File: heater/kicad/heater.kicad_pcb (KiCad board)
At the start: 2 copper layers, 90 x 88.4 mm, 82 parts, among them J1 Conn_01x02_Pin, J2 Conn_01x02_Pin, J3 pcie_98, U1 OPA863SIDBVR, U10 B0509XT-1WR3, U11 ESD5344D-TP, U12 ESD5344D-TP, U13 XC6206P332MR, U2 OPA863SIDBVR, U3 LTC1968, U4 LTC1968, U5 OPA863SIDBVR, U6 OPA863SIDBVR, U7 LP2985-5.0, U8 ADS1115IDGS, U9 ISO1541

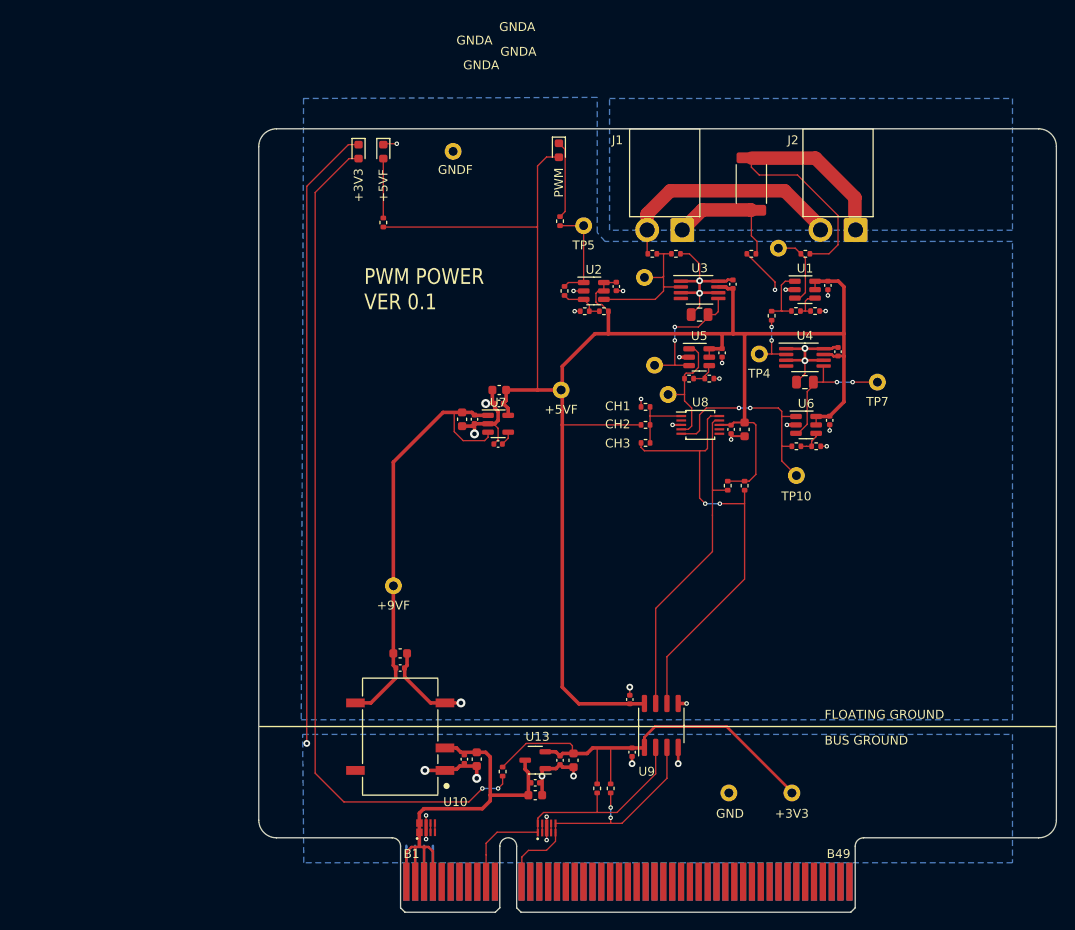
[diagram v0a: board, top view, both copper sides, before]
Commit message: Updated heater layout. Silk screeen labels are done.
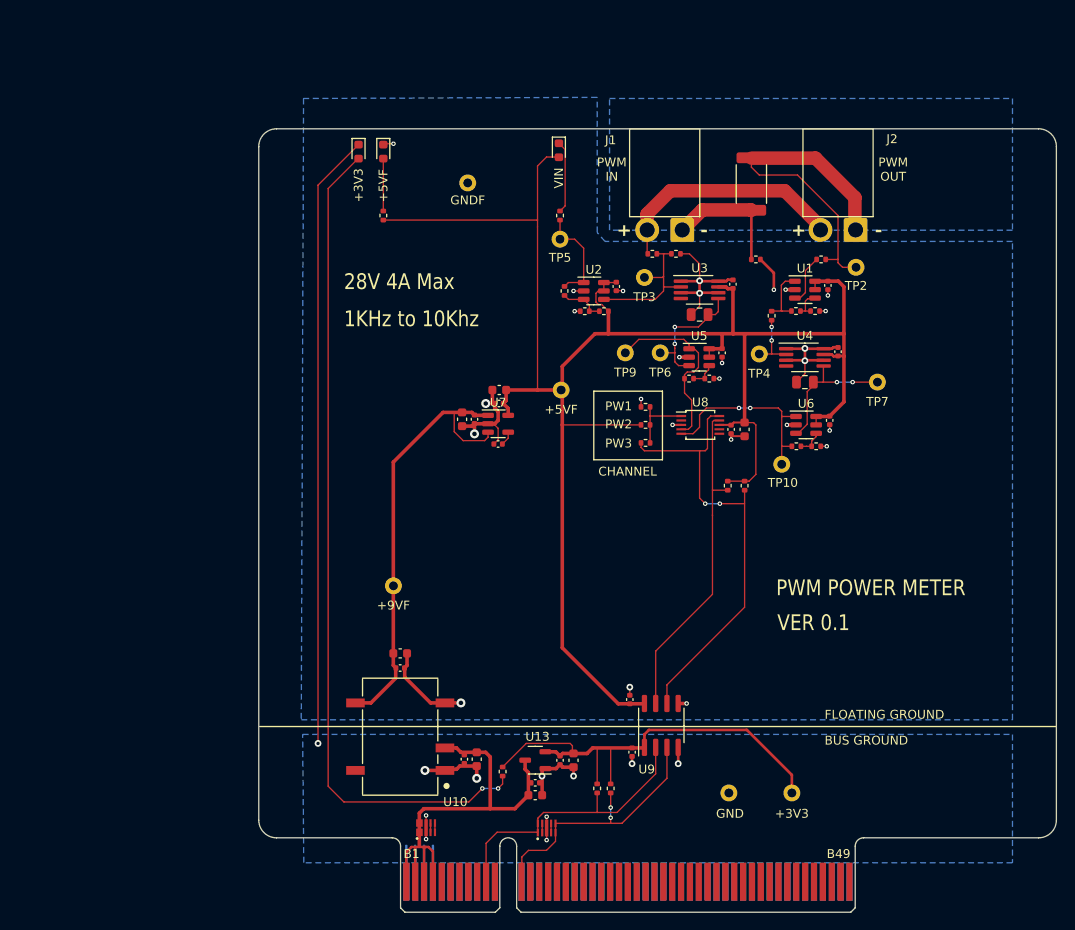
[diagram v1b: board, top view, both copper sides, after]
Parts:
- moved TP2 9.03 mm to (39.2, -72.8)
- moved TP9 6.74 mm to (13.2, -63.1)
- moved TP1 3.92 mm to (-4.57, -82.3)
- moved TP5 3.07 mm to (5.84, -75.9)
- moved TP10 2.08 mm to (30.9, -50.5)
- moved R6 1.89 mm to (35.3, -73.7)
- moved TP6 1.53 mm to (17.1, -63.1)
- moved R1 0.81 mm to (27.9, -73.7), turned to 0 degrees
- moved R5 0.79 mm to (-14.1, -78.6)
- moved R13 0.63 mm to (5.84, -78.6)
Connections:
- TP2 pad 1: Net-(U1-+) -> Net-(J2-Pin_1)
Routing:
- net Net-(U8-AIN0): track 14.1 -> 20.8 mm
- net Net-(U1-+): track 8.83 -> 5.71 mm
- net +5VF: track 211.4 -> 208.8 mm
- net Net-(U8-AIN1): track 24.4 -> 22.2 mm
- net Net-(J2-Pin_1): track 37.2 -> 39.2 mm
- net Net-(D3-A): track 96.2 -> 94.4 mm
- net GNDF: track 79.7 -> 78.0 mm
- net GND: track 109.8 -> 108.6 mm
- net +5V: track 49.6 -> 50.7 mm
- net +3V3: track 51.0 -> 52.0 mm
- net Net-(U3-OUT): track 15.1 -> 14.3 mm
- net Net-(D1-A): track 6.70 -> 5.92 mm
- net Net-(D2-K): track 8.81 -> 8.17 mm
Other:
- board text added: "+"
- board text added: "-"
- board text added: "1KHz to 10Khz"
- board text added: "28V 4A Max"
- board text added: "CHANNEL"
- board text added: "PW1"
- board text added: "PW2"
- board text added: "PW3"
- board text added: "PWM IN"
- board text added: "PWM OUT"
- board text added: "PWM POWER METER"
- board text added: "TO9"
- board text added: "TP2"
- board text added: "TP3"
- board text added: "TP6"
- board text added: "TP9"
- board text added: "VER 0.1"
- board text added: "VIN"
- board text removed: "CH1"
- board text removed: "CH2"
- board text removed: "CH3"
- board text removed: "GNDA"
- board text removed: "PWM"
- board text removed: "PWM POWER VER 0.1"

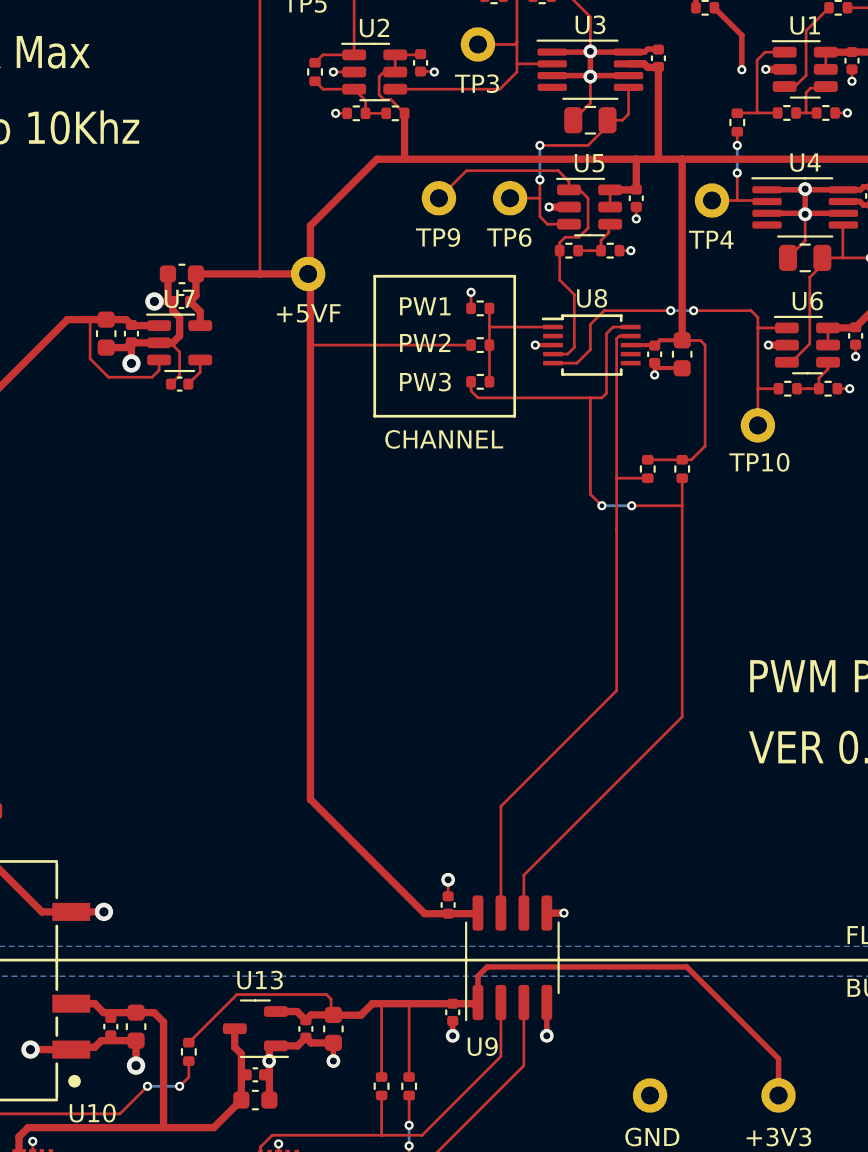
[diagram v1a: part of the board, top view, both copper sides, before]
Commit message: Adjusted for JLCPCB upload.
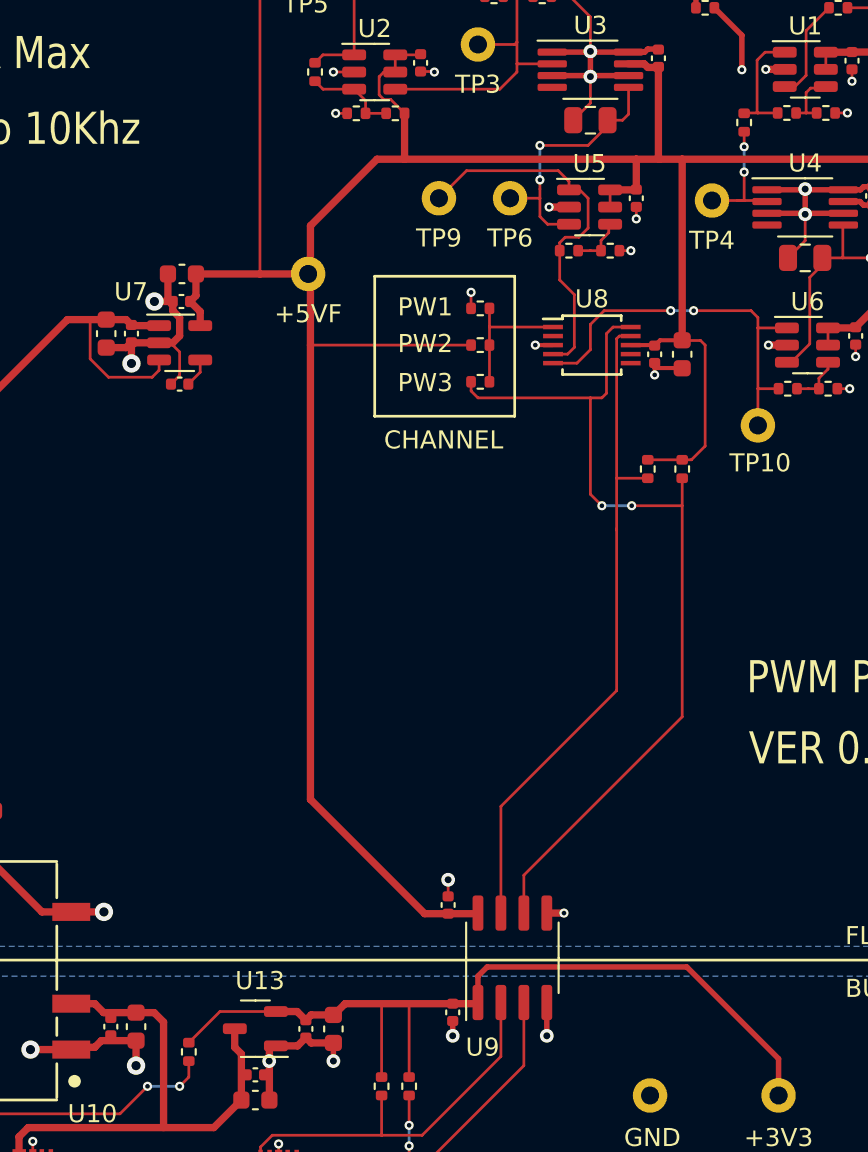
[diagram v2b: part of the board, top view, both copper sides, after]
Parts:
- moved R12 0.38 mm to (30.1, -67.3)
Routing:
- net +3V3: track 52.0 -> 47.7 mm
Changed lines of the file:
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@@
   )
   (footprint "Resistor_SMD:R_0402_1005Metric" (layer "F.Cu")
-    (at 29.718 -67.31 90)
+    (at 30.099 -67.31 90)
     (descr "Resistor SMD 0402 (1005 Metric), square (rectangular) end terminal, IPC_7351 nominal, (Body size source: IPC-SM-782 page 72, https://www.pcb-3d.com/wordpress/wp-content/uploads/ipc-sm-782a_amendment_1_and_2.pdf), generated with kicad-footprint-generator")
     (tags "resistor")
@@
     (descr "Isolated 1W or 2W Single Output SM DC/DC Converters https://www.murata.com/products/productdata/8807031865374/kdc-nxe1.pdf#page=8 https://www.murata.com/products/productdata/8807031898142/kdc-nxe2.pdf#page=9")
     (tags "Isolated 1W or 2W Single Output SM DC/DC Converters")
+    (property "JLCRotOffset" "270")
+    (property "LCSC" "C976389")
     (property "Sheetfile" "heater.kicad_sch")
     (property "Sheetname" "")
@@
     (descr "SOT, 5 Pin (https://www.jedec.org/sites/default/files/docs/Mo-178c.PDF variant AA), generated with kicad-footprint-generator ipc_gullwing_generator.py")
     (tags "SOT TO_SOT_SMD")
+    (property "JLCRotOffset" "180")
     (property "LCSC" "C130188")
     (property "Sheetfile" "heater.kicad_sch")
@@
     (property "ki_keywords" "LDO regulator linear  SOT-23-5")
     (attr smd)
-    (fp_text reference "U7" (at 0 -2.4) (layer "F.SilkS")
+    (fp_text reference "U7" (at -2.6924 -2.8194) (layer "F.SilkS")
         (effects (font (size 1 1) (thickness 0.15)))
     )
@@
     (descr "TSSOP10: plastic thin shrink small outline package; 10 leads; body width 3 mm; (see NXP SSOP-TSSOP-VSO-REFLOW.pdf and sot552-1_po.pdf)")
     (tags "SSOP 0.5")
+    (property "LCSC" "Digikey")
     (property "Sheetfile" "heater.kicad_sch")
     (property "Sheetname" "")
@@
     (descr "SOT, 3 Pin (https://www.jedec.org/sites/default/files/docs/Mo-178D.PDF inferred 3-pin variant), generated with kicad-footprint-generator ipc_gullwing_generator.py")
     (tags "SOT TO_SOT_SMD")
-    (property "LCSC" "C14289")
+    (property "JLCRotOffset" "180")
+    (property "LCSC" "C5446")
     (property "Sheetfile" "heater.kicad_sch")
     (property "Sheetname" "")
@@
     (descr "SOIC, 8 Pin (JEDEC MS-012AA, https://www.analog.com/media/en/package-pcb-resources/package/pkg_pdf/soic_narrow-r/r_8.pdf), generated with kicad-footprint-generator ipc_gullwing_generator.py")
     (tags "SOIC SO")
+    (property "JLCRotOffset" "270")
     (property "Sheetfile" "heater.kicad_sch")
     (property "Sheetname" "")
@@
   (segment (start -9.525 -11.684) (end 0.749 -11.684) (width 0.4064) (layer "F.Cu") (net 2))
   (segment (start -5.842 -18.542) (end -7.142 -18.542) (width 0.4064) (layer "F.Cu") (net 2))
-  (segment (start 7.239 -18.796) (end 6.985 -19.05) (width 0.1524) (layer "F.Cu") (net 3))
+  (segment (start 4.1855 -18.108) (end 1.088 -18.108) (width 0.1524) (layer "F.Cu") (net 3))
   (segment (start 6.137 -17.92) (end 5.842 -17.625) (width 0.4064) (layer "F.Cu") (net 3))
   (segment (start 11.557 -14.482) (end 11.557 -18.542) (width 0.1524) (layer "F.Cu") (net 3))
@@
   (segment (start 10.033 -14.482) (end 10.033 -18.542) (width 0.1524) (layer "F.Cu") (net 3))
   (segment (start 15.875 -20.574) (end 26.924 -20.574) (width 0.3048) (layer "F.Cu") (net 3))
-  (segment (start 6.985 -19.05) (end 2.03 -19.05) (width 0.1524) (layer "F.Cu") (net 3))
   (segment (start 15.367 -18.542) (end 14.035 -18.542) (width 0.4064) (layer "F.Cu") (net 3))
   (segment (start 15.367 -20.066) (end 15.875 -20.574) (width 0.3048) (layer "F.Cu") (net 3))
+  (segment (start 13.97 -18.542) (end 8.014 -18.542) (width 0.4064) (layer "F.Cu") (net 3))
   (segment (start 5.359 -18.108) (end 5.842 -17.625) (width 0.4064) (layer "F.Cu") (net 3))
   (segment (start 32.004 -15.494) (end 32.004 -13.589) (width 0.3048) (layer "F.Cu") (net 3))
-  (segment (start 7.239 -18.047) (end 7.239 -18.796) (width 0.1524) (layer "F.Cu") (net 3))
-  (segment (start 8.89 -17.907) (end 7.379 -17.907) (width 0.4064) (layer "F.Cu") (net 3))
-  (segment (start 13.97 -18.542) (end 9.525 -18.542) (width 0.4064) (layer "F.Cu") (net 3))
-  (segment (start 9.525 -18.542) (end 8.89 -17.907) (width 0.4064) (layer "F.Cu") (net 3))
+  (segment (start 8.014 -18.542) (end 7.379 -17.907) (width 0.4064) (layer "F.Cu") (net 3))
+  (segment (start 1.088 -18.108) (end -0.635 -16.385) (width 0.1524) (layer "F.Cu") (net 3))
   (segment (start 4.1855 -18.108) (end 5.359 -18.108) (width 0.4064) (layer "F.Cu") (net 3))
   (segment (start 7.366 -17.92) (end 6.137 -17.92) (width 0.4064) (layer "F.Cu") (net 3))
-  (segment (start 2.03 -19.05) (end -0.635 -16.385) (width 0.1524) (layer "F.Cu") (net 3))
   (segment (start 26.924 -20.574) (end 32.004 -15.494) (width 0.3048) (layer "F.Cu") (net 3))
   (segment (start 20.64 -67.437) (end 21.59 -68.387) (width 0.1524) (layer "F.Cu") (net 4))
@@
   (segment (start 9.146 -68.5225) (end 8.5145 -69.154) (width 0.1524) (layer "F.Cu") (net 113))
   (segment (start 6.792 -69.154) (end 8.5145 -69.154) (width 0.1524) (layer "F.Cu") (net 113))
-  (segment (start 29.7355 -67.8375) (end 29.718 -67.82) (width 0.1524) (layer "F.Cu") (net 114))
   (segment (start 31.9535 -67.8375) (end 30.861 -67.8375) (width 0.1524) (layer "F.Cu") (net 114))
   (segment (start 30.8145 -67.884) (end 30.861 -67.8375) (width 0.1524) (layer "F.Cu") (net 114))
+  (segment (start 30.1165 -67.8375) (end 30.099 -67.82) (width 0.1524) (layer "F.Cu") (net 114))
   (segment (start 32.344 -71.2005) (end 31.2565 -71.2005) (width 0.1524) (layer "F.Cu") (net 114))
-  (segment (start 30.861 -67.8375) (end 29.7355 -67.8375) (width 0.1524) (layer "F.Cu") (net 114))
   (segment (start 31.2565 -71.2005) (end 30.8145 -70.7585) (width 0.1524) (layer "F.Cu") (net 114))
+  (segment (start 30.861 -67.8375) (end 30.1165 -67.8375) (width 0.1524) (layer "F.Cu") (net 114))
   (segment (start 30.8145 -70.7585) (end 30.8145 -67.884) (width 0.1524) (layer "F.Cu") (net 114))
   (segment (start 6.788 -71.054) (end 6.35 -70.616) (width 0.1524) (layer "F.Cu") (net 115))
@@
   (segment (start 5.842 -78.103) (end 5.842 -75.946) (width 0.1524) (layer "F.Cu") (net 115))
   (segment (start 29.718 -62.992) (end 28.321 -62.992) (width 0.1524) (layer "F.Cu") (net 116))
-  (segment (start 29.718 -64.516) (end 29.718 -62.992) (width 0.1524) (layer "F.Cu") (net 116))
+  (segment (start 30.099 -62.992) (end 30.099 -64.5668) (width 0.1524) (layer "F.Cu") (net 116))
+  (segment (start 29.718 -62.992) (end 30.099 -62.992) (width 0.1524) (layer "F.Cu") (net 116))
   (segment (start 31.3075 -62.992) (end 29.718 -62.992) (width 0.1524) (layer "F.Cu") (net 116))
+  (segment (start 30.099 -66.8) (end 30.099 -65.963798) (width 0.1524) (layer "F.Cu") (net 116))
   (segment (start 31.3635 -62.936) (end 31.3075 -62.992) (width 0.1524) (layer "F.Cu") (net 116))
-  (segment (start 29.718 -66.8) (end 29.718 -66.04) (width 0.1524) (layer "F.Cu") (net 116))
-  (via (at 29.718 -66.04) (size 0.508) (drill 0.254) (layers "F.Cu" "B.Cu") (net 116))
-  (via (at 29.718 -64.516) (size 0.508) (drill 0.254) (layers "F.Cu" "B.Cu") (net 116))
-  (segment (start 29.718 -66.04) (end 29.718 -64.516) (width 0.1524) (layer "B.Cu") (net 116))
+  (via (at 30.099 -65.963798) (size 0.508) (drill 0.254) (layers "F.Cu" "B.Cu") (net 116))
+  (via (at 30.099 -64.5668) (size 0.508) (drill 0.254) (layers "F.Cu" "B.Cu") (net 116))
+  (segment (start 30.099 -64.5668) (end 30.099 -65.963798) (width 0.1524) (layer "B.Cu") (net 116))
   (segment (start 22.5595 -61.559) (end 22.681 -61.6805) (width 0.1524) (layer "F.Cu") (net 117))
   (segment (start 20.7835 -60.2175) (end 21.59 -60.2175) (width 0.1524) (layer "F.Cu") (net 117))

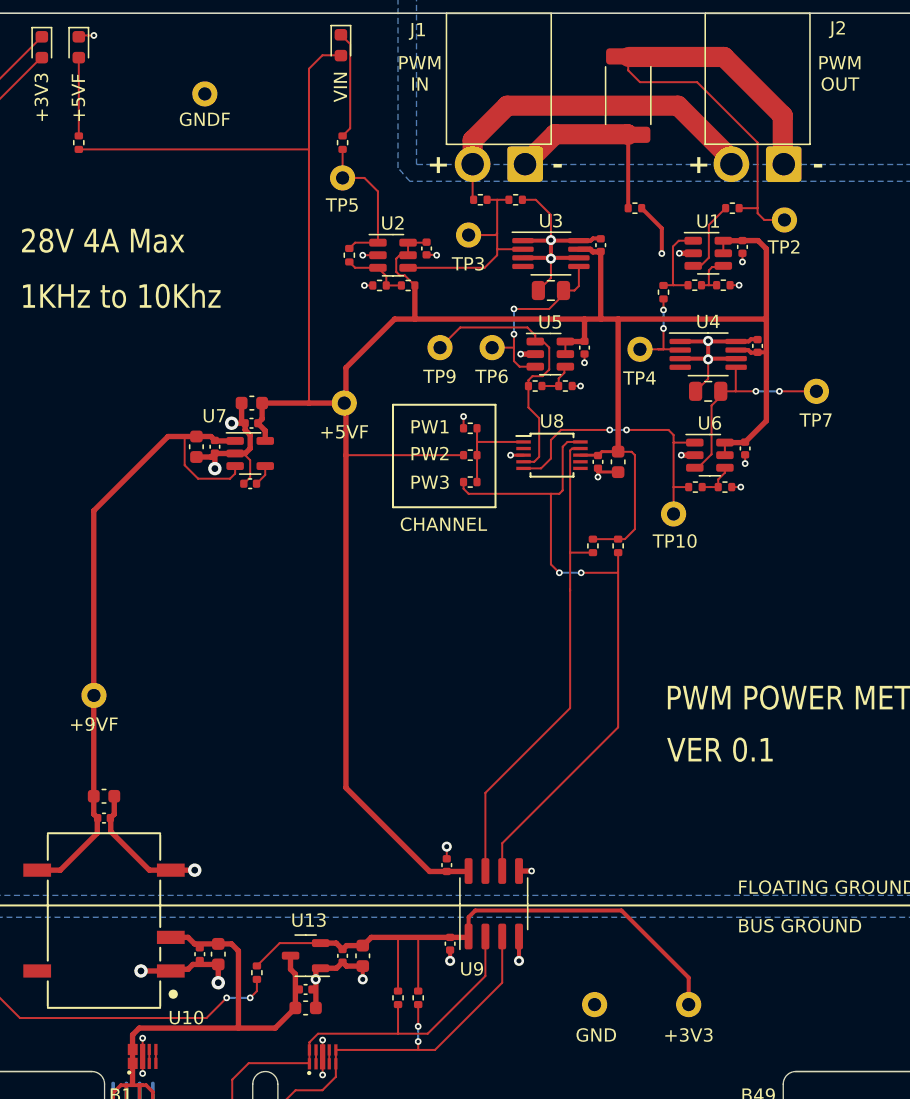
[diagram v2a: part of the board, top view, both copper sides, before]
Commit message: Increased the hole of the test point footprint.
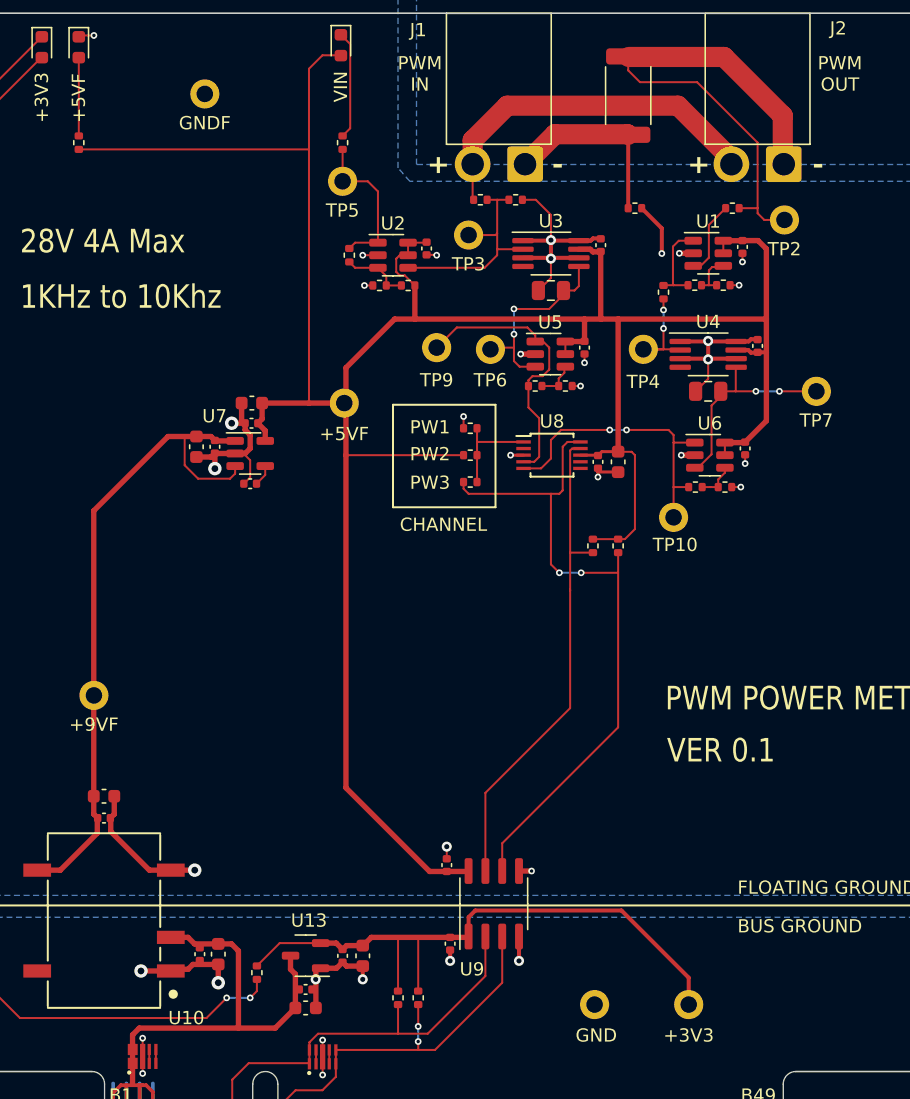
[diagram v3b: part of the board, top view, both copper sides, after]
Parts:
- moved TP5 0.25 mm to (5.84, -75.7)
- moved TP9 0.25 mm to (13.0, -63.1)
- moved TP10 0.25 mm to (30.9, -50.3)
- moved TP4 0.25 mm to (28.6, -63.0)
- moved TP6 0.18 mm to (17.0, -63.0)
